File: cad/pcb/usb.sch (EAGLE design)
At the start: 25 parts, among them Q1 ZXMP6A13FTA, Q2 mmbt2222, Q3 mmbt2222, U1 MIC5225-3.3v, U2 CH340C, U3 MCP73831T-2ACI/OT, X1 SM02B-SRSS-TB

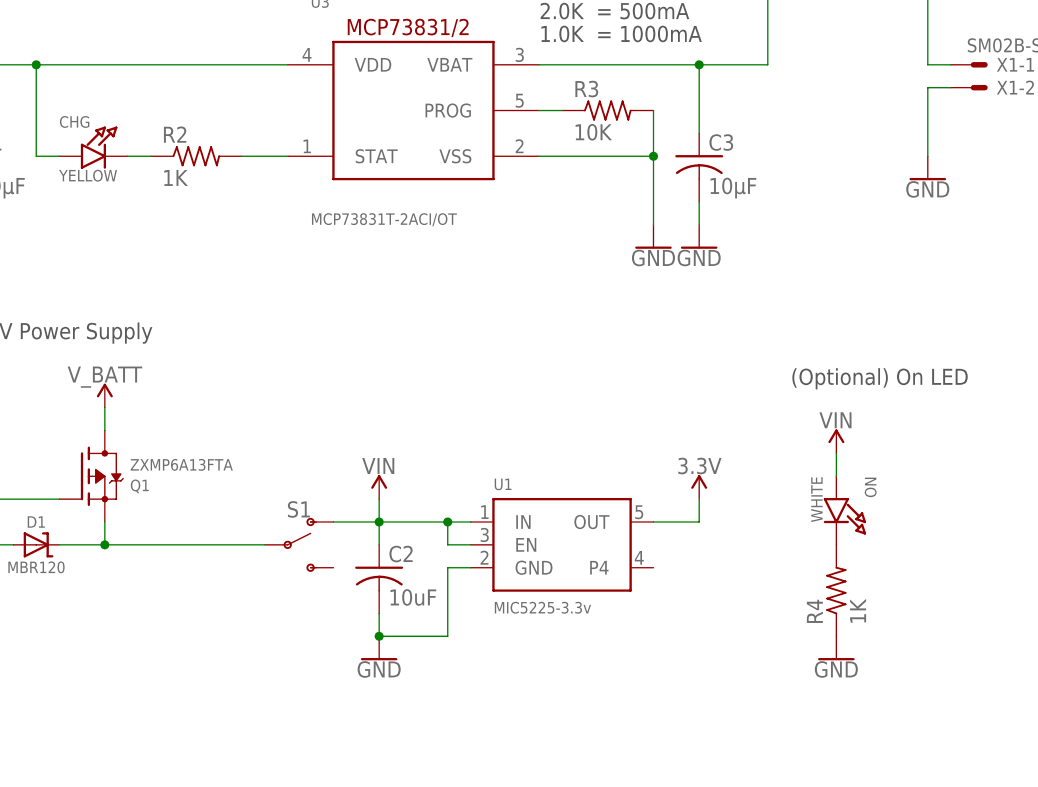
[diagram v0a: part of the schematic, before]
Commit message: updated R2 and R4 values, changed 3.3v regulator to AP2112K-3.3
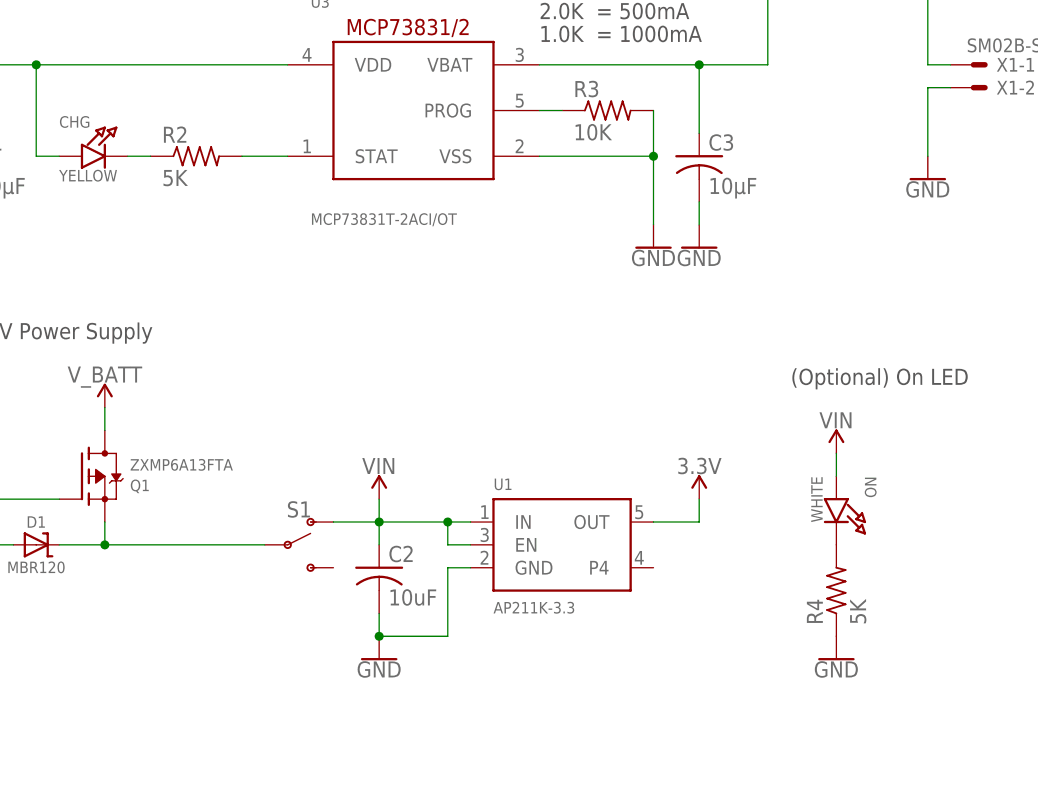
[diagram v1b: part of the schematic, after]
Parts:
- R2, R4: value 1K -> 5K; MPN ESR10EZPJ102 -> 0805W8F4871T5E
- U1: value MIC5225-3.3v -> AP211K-3.3; MPN MIC5225-3.3YM5-TR -> AP2112K-3.3
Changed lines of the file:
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@@
 </classes>
 <parts>
-<part name="U1" library="microbuilder" deviceset="VREG_SOT23-5" device="" value="MIC5225-3.3v">
-<attribute name="MPN" value="MIC5225-3.3YM5-TR"/>
+<part name="U1" library="microbuilder" deviceset="VREG_SOT23-5" device="" value="AP211K-3.3">
+<attribute name="MPN" value="AP2112K-3.3"/>
 </part>
 <part name="U3" library="adafruit" library_urn="urn:adsk.eagle:library:420" deviceset="MCP73831" device="/OT" package3d_urn="urn:adsk.eagle:package:6240724/1" override_package3d_urn="urn:adsk.eagle:package:21520838/2" override_package_urn="urn:adsk.eagle:footprint:6240078/1" value="MCP73831T-2ACI/OT">
@@
 <attribute name="MPN" value="NCD0805W2"/>
 </part>
-<part name="R2" library="adafruit" library_urn="urn:adsk.eagle:library:420" deviceset="R-US_" device="R0805" package3d_urn="urn:adsk.eagle:package:6240566/1" override_package3d_urn="urn:adsk.eagle:package:21520789/2" override_package_urn="urn:adsk.eagle:footprint:6239920/1" value="1K">
-<attribute name="MPN" value="ESR10EZPJ102"/>
+<part name="R2" library="adafruit" library_urn="urn:adsk.eagle:library:420" deviceset="R-US_" device="R0805" package3d_urn="urn:adsk.eagle:package:6240566/1" override_package3d_urn="urn:adsk.eagle:package:21520789/2" override_package_urn="urn:adsk.eagle:footprint:6239920/1" value="5K">
+<attribute name="MPN" value="0805W8F4871T5E"/>
 </part>
 <part name="C1" library="adafruit" library_urn="urn:adsk.eagle:library:420" deviceset="C-US" device="C0805" package3d_urn="urn:adsk.eagle:package:6240337/1" override_package3d_urn="urn:adsk.eagle:package:21520831/3" override_package_urn="urn:adsk.eagle:footprint:6239686/1" value="10µF">
@@
 <attribute name="MPN" value="NCD0805W2"/>
 </part>
-<part name="R4" library="adafruit" library_urn="urn:adsk.eagle:library:420" deviceset="R-US_" device="R0805" package3d_urn="urn:adsk.eagle:package:6240566/1" override_package3d_urn="urn:adsk.eagle:package:21520793/2" override_package_urn="urn:adsk.eagle:footprint:6239920/1" value="1K">
-<attribute name="MPN" value="ESR10EZPJ102"/>
+<part name="R4" library="adafruit" library_urn="urn:adsk.eagle:library:420" deviceset="R-US_" device="R0805" package3d_urn="urn:adsk.eagle:package:6240566/1" override_package3d_urn="urn:adsk.eagle:package:21520793/2" override_package_urn="urn:adsk.eagle:footprint:6239920/1" value="5K">
+<attribute name="MPN" value="0805W8F4871T5E"/>
 </part>
 <part name="R1" library="adafruit" library_urn="urn:adsk.eagle:library:420" deviceset="R-US_" device="R0805" package3d_urn="urn:adsk.eagle:package:6240566/1" override_package3d_urn="urn:adsk.eagle:package:21520834/2" override_package_urn="urn:adsk.eagle:footprint:6239920/1" value="100K">

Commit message: added POPULATE to usb thru hole parts
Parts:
- J2, JP1, JP2: POPULATE (none) -> 1
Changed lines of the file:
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@@
 <part name="JP2" library="adafruit" library_urn="urn:adsk.eagle:library:420" deviceset="PINHD-1X8" device="CLEANBIG" package3d_urn="urn:adsk.eagle:package:6240708/1" override_package3d_urn="urn:adsk.eagle:package:21520758/2" override_package_urn="urn:adsk.eagle:footprint:6240062/1">
 <attribute name="MPN" value="C27438"/>
+<attribute name="POPULATE" value="1"/>
 <attribute name="THRU-HOLE" value="1"/>
 </part>
 <part name="JP1" library="adafruit" library_urn="urn:adsk.eagle:library:420" deviceset="PINHD-1X8" device="CLEANBIG" package3d_urn="urn:adsk.eagle:package:6240708/1" override_package3d_urn="urn:adsk.eagle:package:21520677/2" override_package_urn="urn:adsk.eagle:footprint:6240062/1">
 <attribute name="MPN" value="C27438"/>
+<attribute name="POPULATE" value="1"/>
 <attribute name="THRU-HOLE" value="1"/>
 </part>
@@
 <attribute name="BOTTOM" value="1"/>
 <attribute name="MPN" value="U-D-M5DD-W-1"/>
+<attribute name="POPULATE" value="1"/>
 <attribute name="THRU-HOLE" value="1"/>
 </part>
@@
 <attribute name="MPN" x="58.42" y="20.32" size="1.778" layer="96" rot="R180" display="off"/>
 <attribute name="THRU-HOLE" x="58.42" y="20.32" size="1.778" layer="96" rot="R180" display="off"/>
+<attribute name="POPULATE" x="58.42" y="20.32" size="1.778" layer="96" rot="R180" display="off"/>
 </instance>
 <instance part="JP1" gate="G$1" x="48.26" y="22.86" smashed="yes">
@@
 <attribute name="MPN" x="48.26" y="22.86" size="1.778" layer="96" display="off"/>
 <attribute name="THRU-HOLE" x="48.26" y="22.86" size="1.778" layer="96" display="off"/>
+<attribute name="POPULATE" x="48.26" y="22.86" size="1.778" layer="96" display="off"/>
 </instance>
 <instance part="J2" gate="G$1" x="182.88" y="22.86" smashed="yes">
@@
 <attribute name="THRU-HOLE" x="182.88" y="22.86" size="1.778" layer="96" display="off"/>
 <attribute name="BOTTOM" x="182.88" y="22.86" size="1.778" layer="96" display="off"/>
+<attribute name="POPULATE" x="182.88" y="22.86" size="1.778" layer="96" display="off"/>
 </instance>
 <instance part="D1" gate="G$1" x="25.4" y="68.58" smashed="yes">

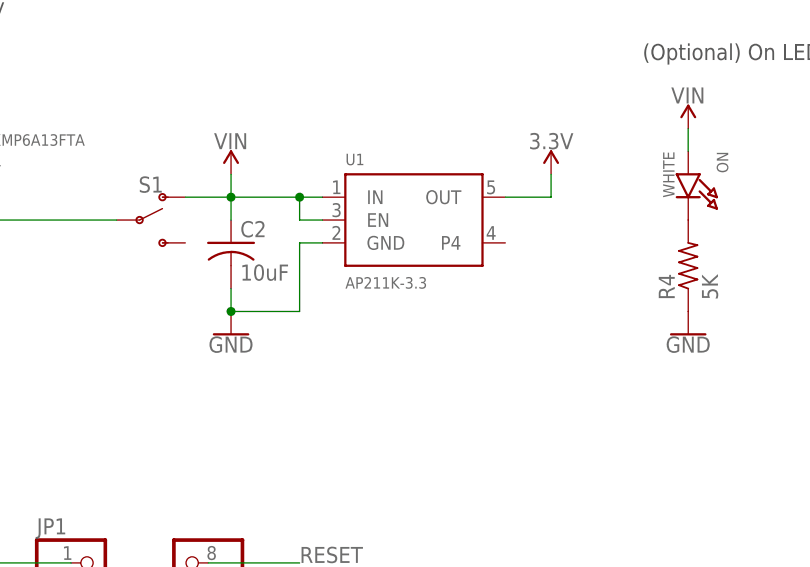
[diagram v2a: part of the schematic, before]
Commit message: fixed part number
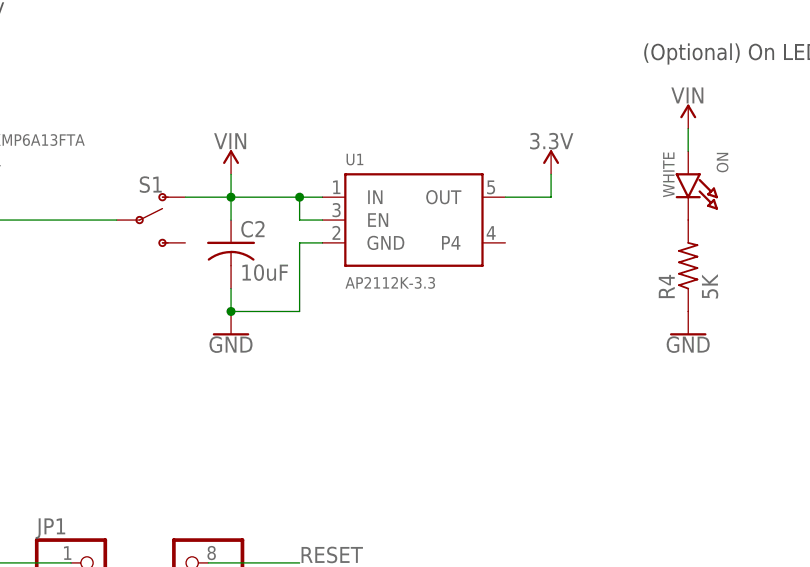
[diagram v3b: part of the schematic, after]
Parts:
- U1: value AP211K-3.3 -> AP2112K-3.3
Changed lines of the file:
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@@
 </classes>
 <parts>
-<part name="U1" library="microbuilder" deviceset="VREG_SOT23-5" device="" value="AP211K-3.3">
+<part name="U1" library="microbuilder" deviceset="VREG_SOT23-5" device="" value="AP2112K-3.3">
 <attribute name="MPN" value="AP2112K-3.3"/>
 </part>

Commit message: renamed yellow led to white
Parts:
- CHG: value YELLOW -> WHITE
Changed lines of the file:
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@@
 <?xml version="1.0" encoding="utf-8"?>
 <!DOCTYPE eagle SYSTEM "eagle.dtd">
-<eagle version="9.6.2">
+<eagle version="9.5.0">
 <drawing>
 <settings>
@@
 <attribute name="MPN" value="MCP73831T-2ACI/OT"/>
 </part>
-<part name="CHG" library="microbuilder" deviceset="LED" device="0805_NOOUTLINE" value="YELLOW">
+<part name="CHG" library="microbuilder" deviceset="LED" device="0805_NOOUTLINE" value="WHITE">
 <attribute name="MPN" value="NCD0805W2"/>
 </part>
